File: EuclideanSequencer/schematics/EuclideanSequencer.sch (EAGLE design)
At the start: 47 parts, among them IC1 MEGA168, Q1 2N3904, Q2 2N3904, Q3 2N3904, Q4 2N3904, Y1 16Mhz

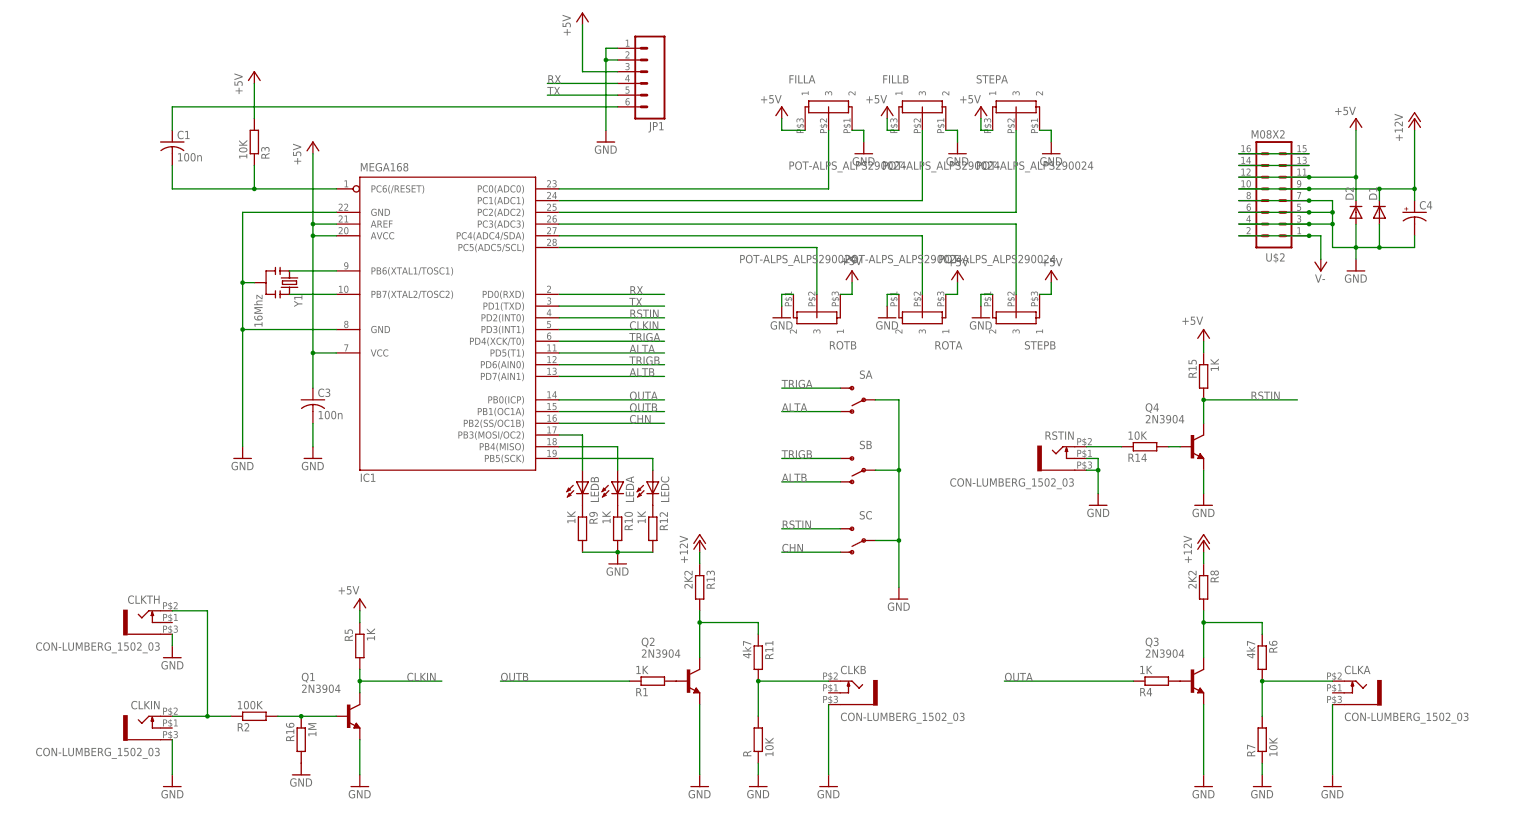
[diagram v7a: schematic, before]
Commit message: added pull-down resistor on RST input, updated resistor values on outputs
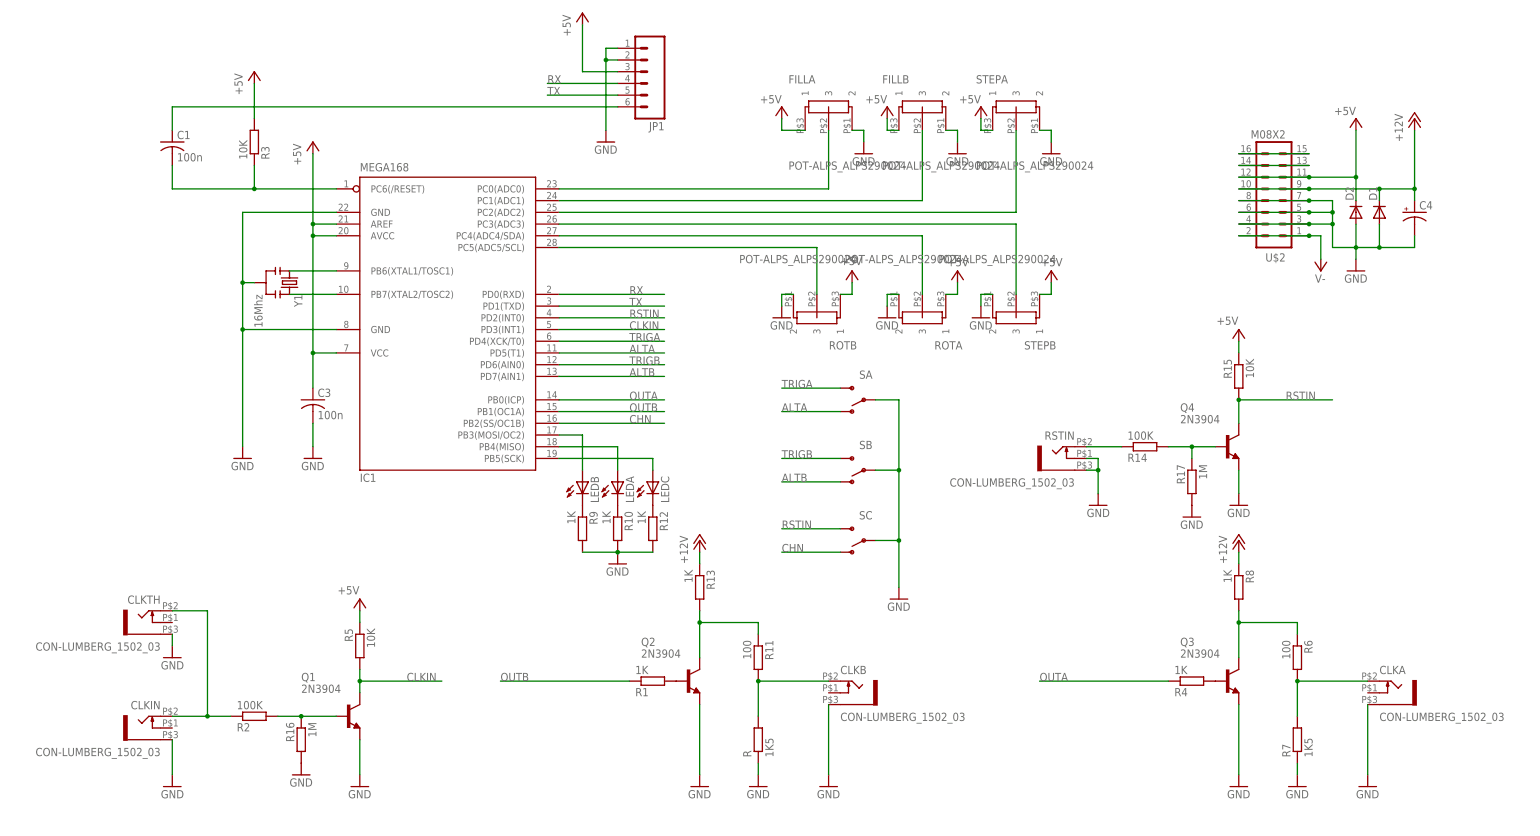
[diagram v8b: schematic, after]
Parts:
- added R17: 1M, rcl:R-EU_0204/7
- R, R7: value 10K -> 1K5
- R11, R6: value 4k7 -> 100
- R13, R8: value 2K2 -> 1K
- R14: value 10K -> 100K
- R15, R5: value 1K -> 10K
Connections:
- net GND: now also R17.2
- net N$32: now also R17.1
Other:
- moved on the sheet: CLKA, Q3, Q4, R15, R4, R6, R7, R8
